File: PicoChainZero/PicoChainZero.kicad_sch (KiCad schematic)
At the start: 37 parts, among them J1 RJ45, J2 RJ45, J3 Raspberry Pi, J4 USB_C_Receptacle_USB2.0_14P, J5 +12V In, J6 +24V In, U1 LM78M05, U2 FT232RL, U3 SRV05, U4 PCA9615DP, U5 SRV05, U6 SiP32419, U8 SiP32419

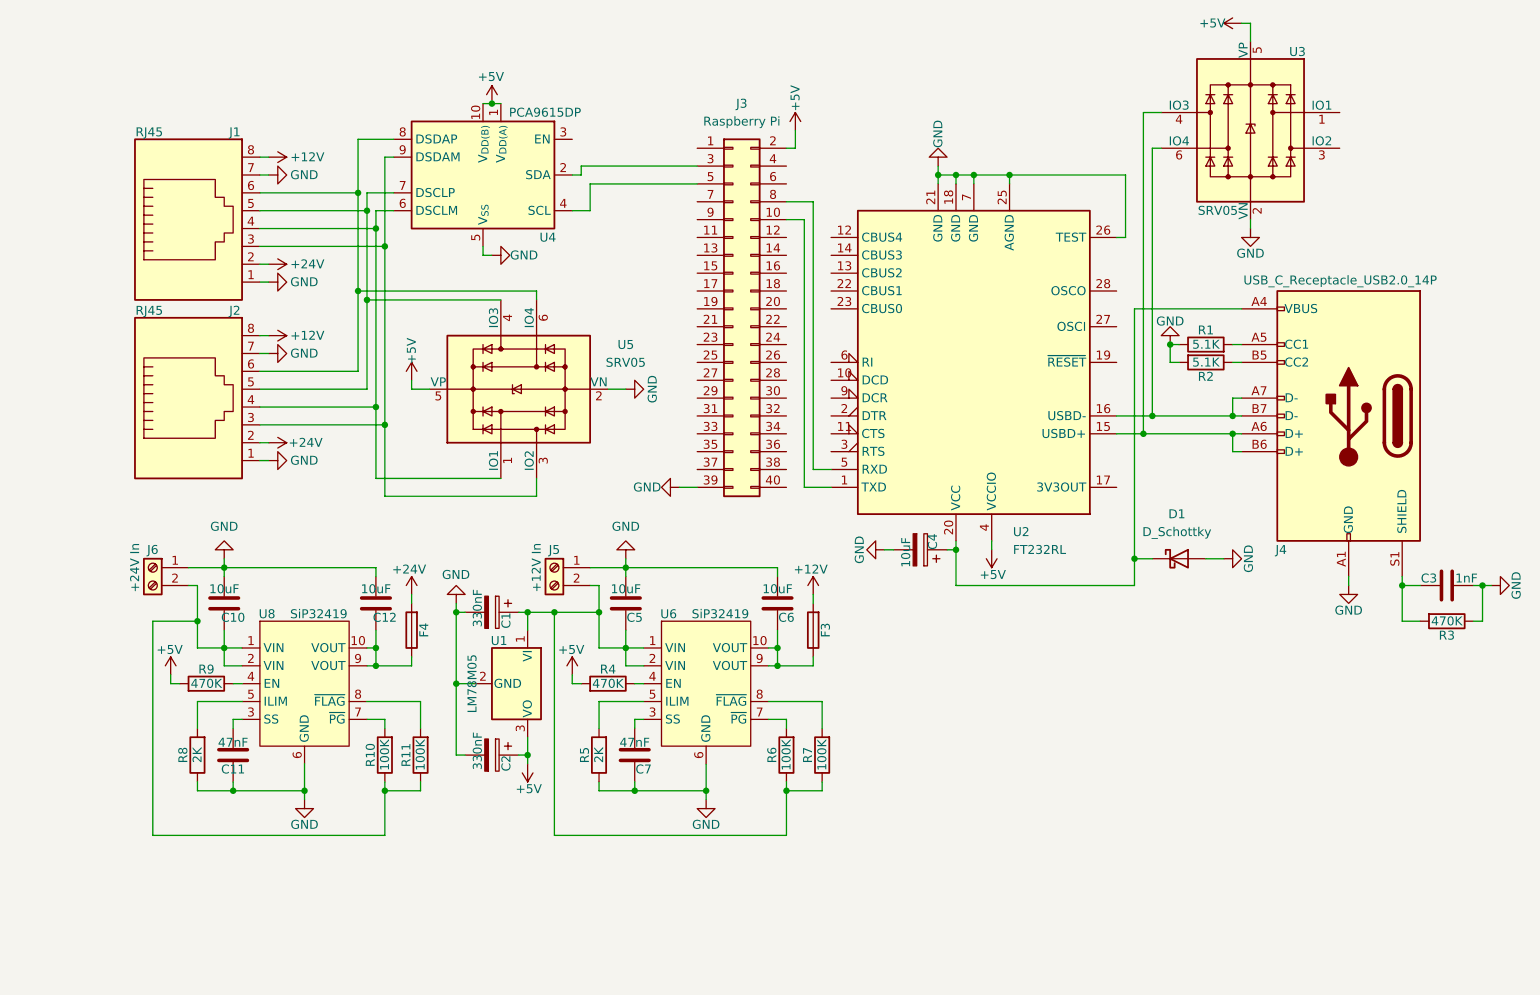
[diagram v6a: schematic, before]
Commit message: Added decoupling capacitors to dI2C drivers (doh)
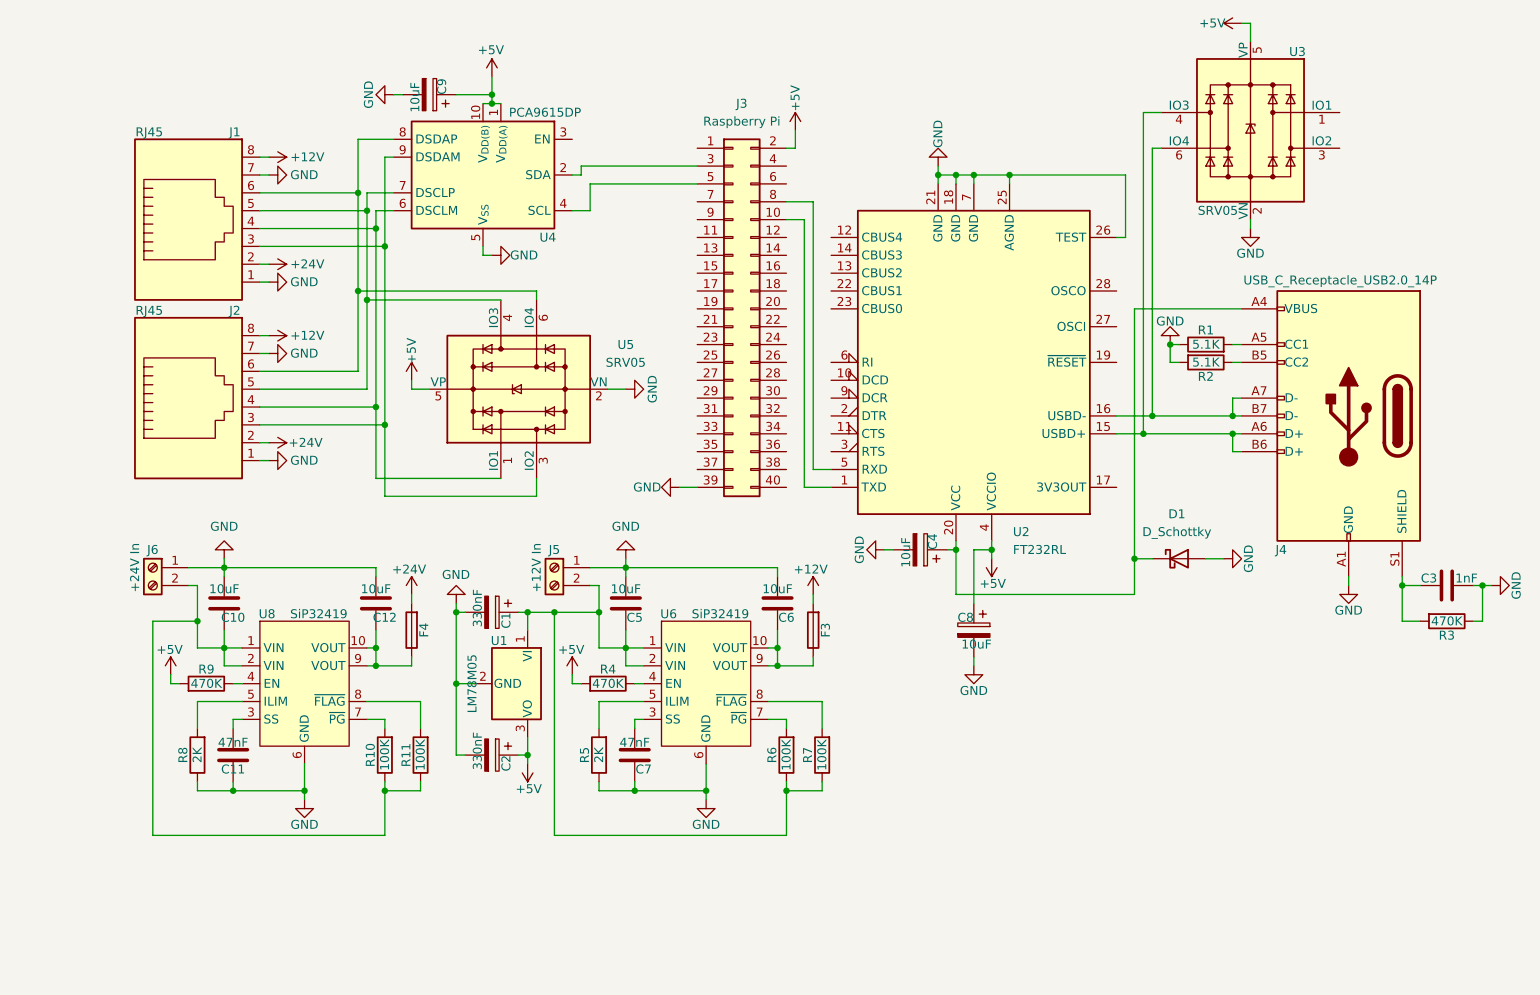
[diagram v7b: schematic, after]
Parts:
- added C8, C9: 10uF, Capacitor_Tantalum_SMD:CP_EIA-3216-18_Kemet-A, symbol Device:C_Polarized
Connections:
- net +5V: now also C8.1, C9.1
- net GND: now also C8.2, C9.2

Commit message: Adjustments to PicoChainZero
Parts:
- added J7, J8: Conn_01x02_Pin, Connector_PinHeader_2.54mm:PinHeader_1x02_P2.54mm_Vertical, symbol Connector:Conn_01x02_Pin
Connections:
- net +12V: now also J8.1 (Pin_1)
- net +24V: now also J7.1 (Pin_1)
- net GND: now also J3.14 (Pin_14), J3.20 (Pin_20), J3.25 (Pin_25), J3.30 (Pin_30), J3.34 (Pin_34), J3.6 (Pin_6), J3.9 (Pin_9)
- net at C1.1, C5.2, J5.2 (Pin_2)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: now also J8.2 (Pin_2)
- net at C10.2, J6.2 (Pin_2), R10.1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: now also J7.2 (Pin_2)
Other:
- moved on the sheet: C1, C2, C5, C6, C7, F3, J5, R4, R5, R6, R7, U1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
